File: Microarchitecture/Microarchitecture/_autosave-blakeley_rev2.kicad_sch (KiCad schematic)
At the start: 11 parts

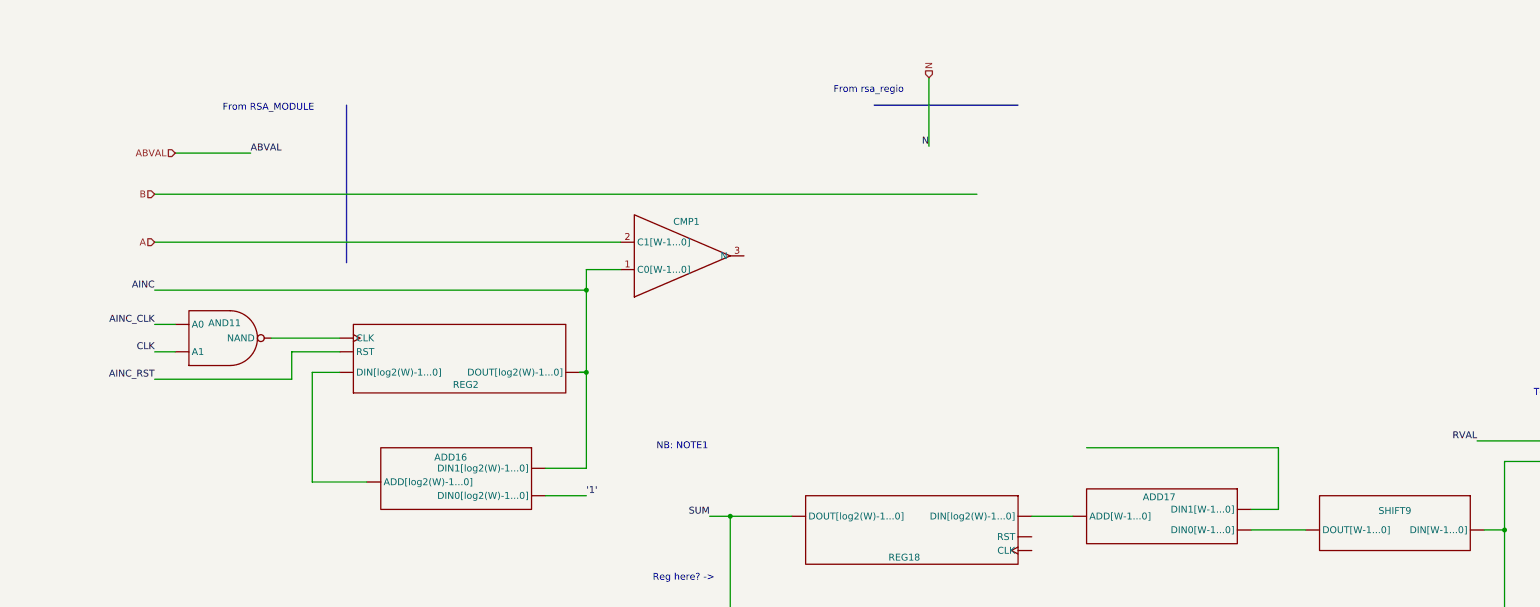
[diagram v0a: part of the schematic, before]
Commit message: Error only on max bits, python problem?
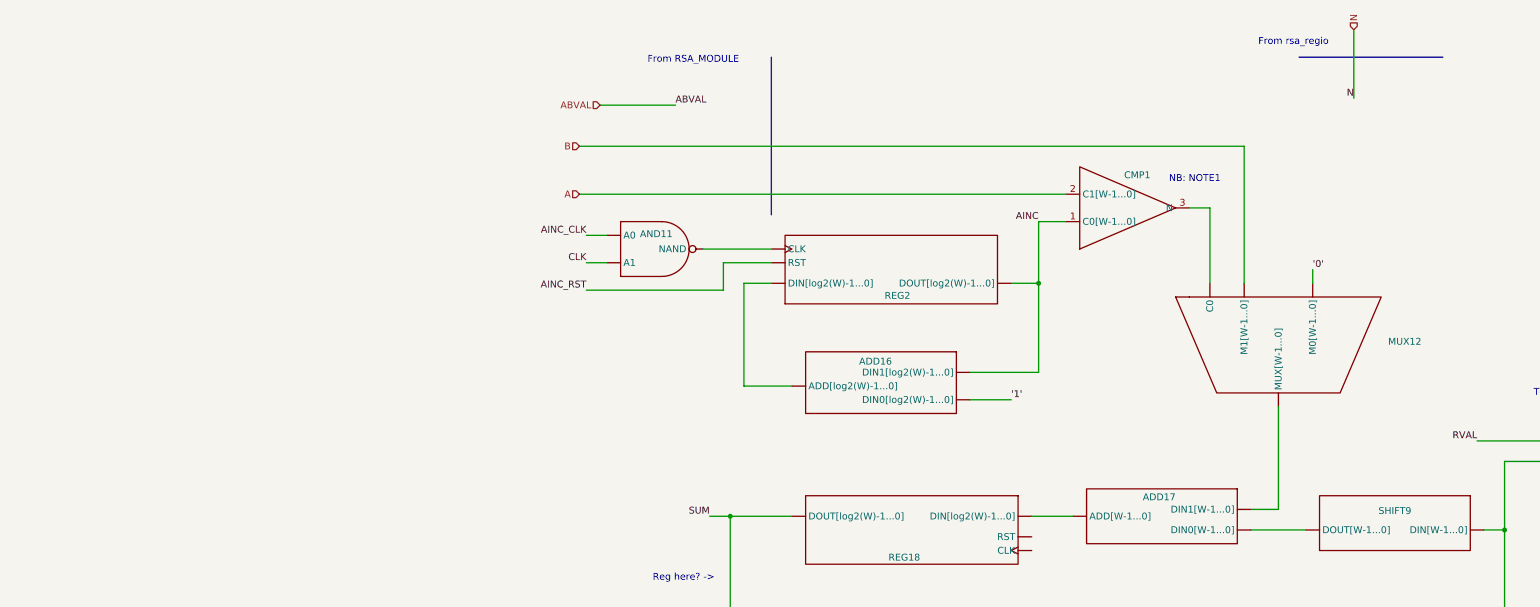
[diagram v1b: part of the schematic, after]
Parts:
- added MUX12: ~, symbol Symbols:MUX_BUS
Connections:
- net B: now also MUX12. (MUX[W-1...0])
- net at CMP1.3 (N): now also MUX12. (MUX[W-1...0])
- net at ADD17. (DIN1[W-1...0]): now also SHIFT9. (DOUT[W-1...0])
- new net: MUX11. (MUX[W-1...0]), SUB12. (SUB[W-1...0])
- new net: MUX11. (MUX[W-1...0]), SUB8. (SUB[W-1...0])
- new net: ADD17. (DIN1[W-1...0]), MUX12. (MUX[W-1...0])
- new net: ADD17. (DIN1[W-1...0]), REG18. (RST)
- new net: AND11. (NAND), REG2. (RST)
- new net: ADD16. (DIN1[log2(W)-1...0]), REG2. (RST)
- new net '0': MUX12. (MUX[W-1...0])
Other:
- moved on the sheet: ADD16, AND11, CMP1, REG2

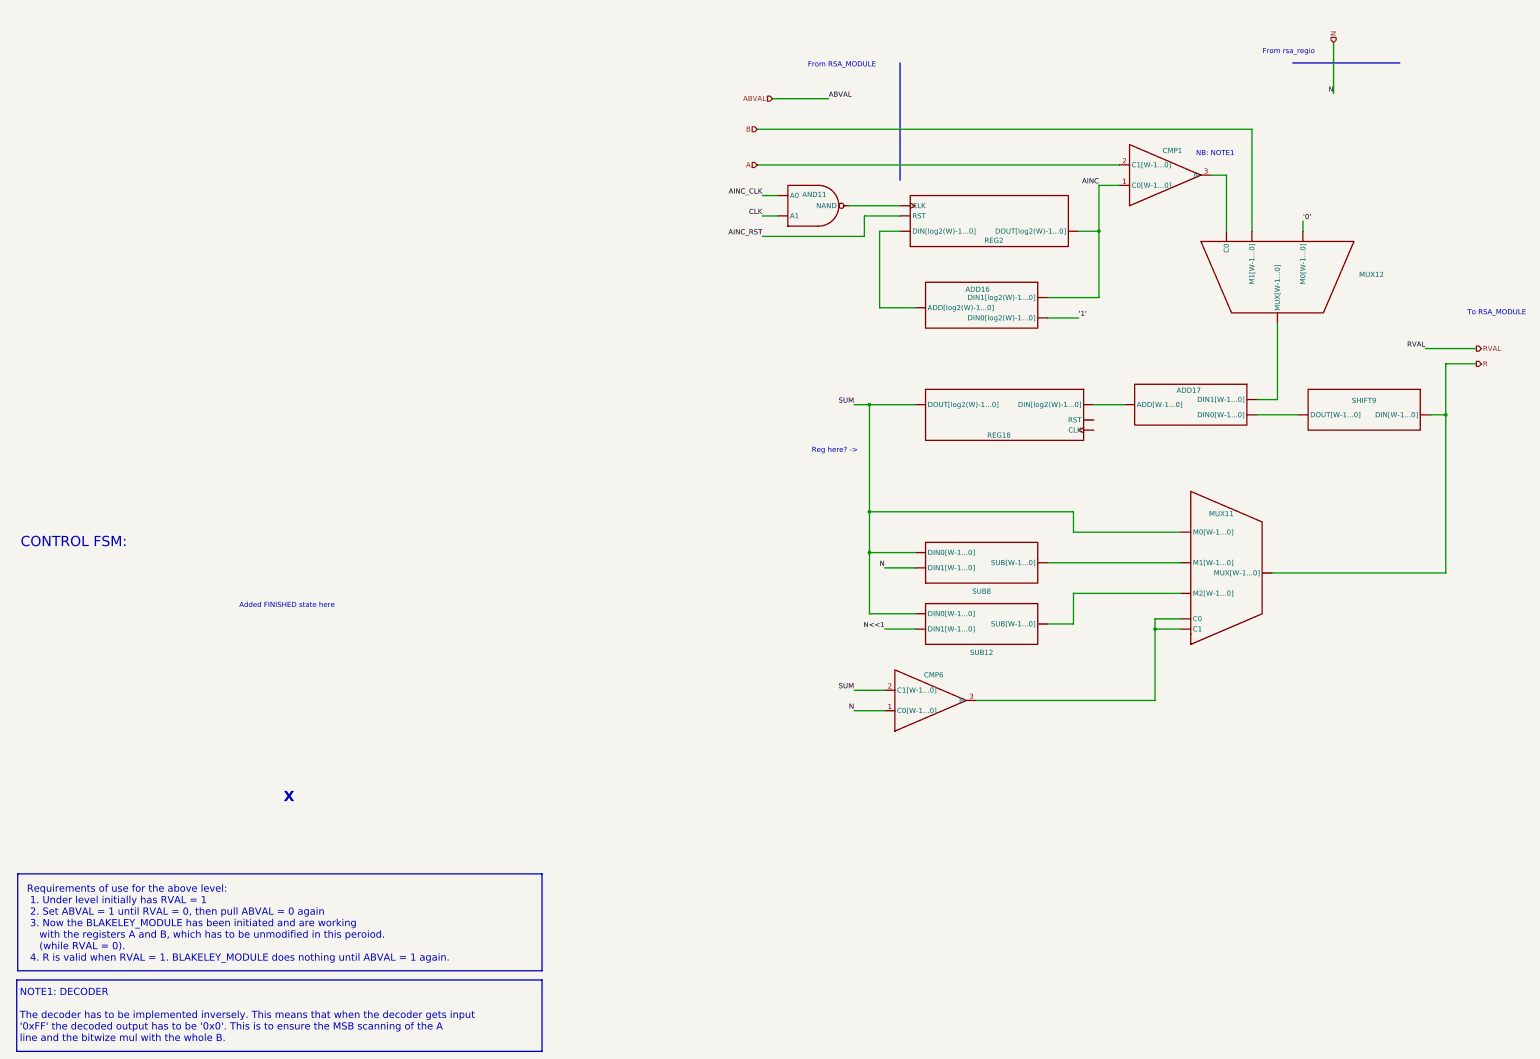
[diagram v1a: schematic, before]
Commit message: Fixed overflow when sll, 100% working
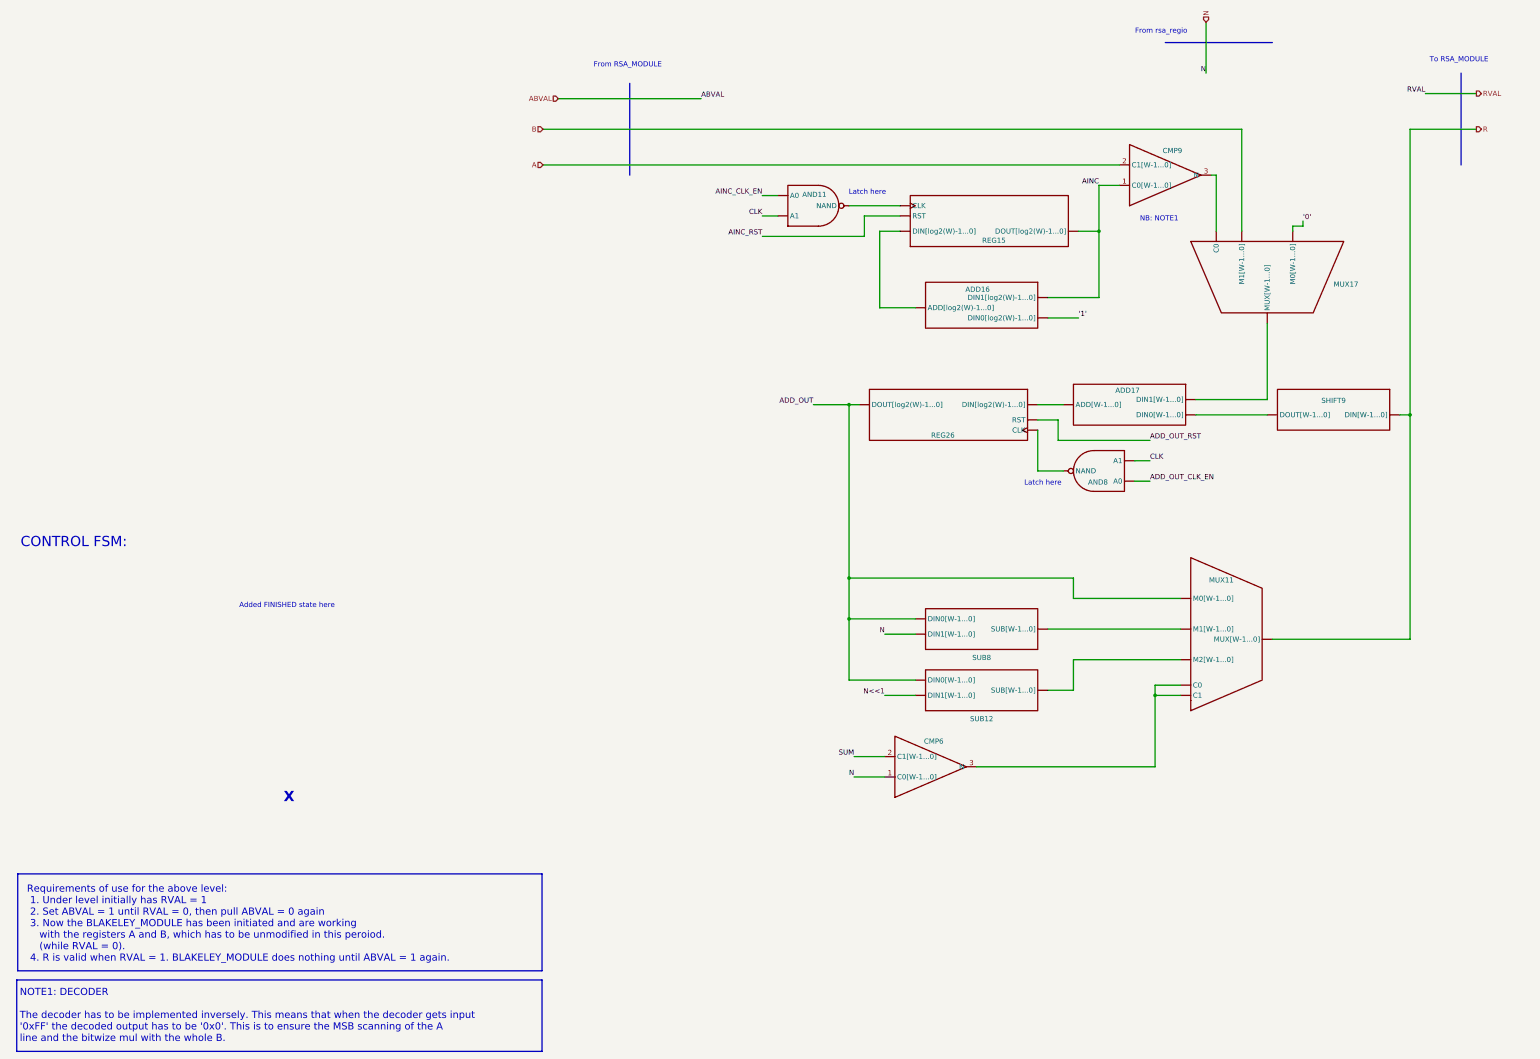
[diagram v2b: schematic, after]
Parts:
- added AND8: ~, symbol Symbols:AND
- renumbered CMP1 to CMP9, MUX12 to MUX17, REG2 to REG15, REG18 to REG26
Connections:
- net AINC_CLK is gone; now on net CLK: AND11. (NAND)
- net CLK: now also AND8. (NAND)
- net SUM: no longer MUX11. (MUX[W-1...0]), REG26. (RST), SUB12. (SUB[W-1...0]), SUB8. (SUB[W-1...0])
- net at ADD17. (DIN1[W-1...0]): now also SHIFT9. (DOUT[W-1...0]); no longer MUX17. (MUX[W-1...0])
- net ADD_OUT_RST: now reaches REG26. (RST)
- net ADD_OUT_RST: no longer ADD17. (DIN1[W-1...0])
- new net: MUX11. (MUX[W-1...0]), SUB12. (SUB[W-1...0])
- new net: AND8. (NAND), REG26. (RST)
- new net: MUX11. (MUX[W-1...0]), SUB8. (SUB[W-1...0])
- new net: ADD17. (DIN1[W-1...0]), MUX17. (MUX[W-1...0])
- new net: ADD17. (DIN1[W-1...0]), REG26. (RST)
- new net: AND11. (NAND), REG15. (RST)
- new net: ADD16. (DIN1[log2(W)-1...0]), REG15. (RST)
- new net ADD_OUT: MUX11. (MUX[W-1...0]), REG26. (RST), SUB12. (SUB[W-1...0]), SUB8. (SUB[W-1...0])
- new net ADD_OUT_CLK_EN: AND8. (NAND)
- new net AINC_CLK_EN: AND11. (NAND)
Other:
- note added: "Latch here"
- note removed: "Reg here? ->"
- moved on the sheet: ADD17, CMP6, MUX11, MUX17, REG26, SHIFT9, SUB12, SUB8
